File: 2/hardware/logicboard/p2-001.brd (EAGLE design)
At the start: 72 x 72 mm, 68 parts, among them IC1 74LS06N, IC101 74LS153D, IC102 LTC485S, IC103 LTC485S, IC2 4066N, J1 MKR, J101 Qwiic, J102 Qwiic, J103 Qwiic, J104 Qwiic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

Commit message: Clean up of schematic.
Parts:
- J20: value (none) -> GPIO
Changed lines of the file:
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@@
 <attribute name="VALUE" x="54.849" y="68.54" size="0.6096" layer="27" font="vector" ratio="20"/>
 </element>
-<element name="J20" library="SparkFun-Connectors" library_urn="urn:adsk.eagle:library:513" package="1X04_1.27MM" package3d_urn="urn:adsk.eagle:package:38086/1" value="" x="25.65" y="69" smashed="yes">
+<element name="J20" library="SparkFun-Connectors" library_urn="urn:adsk.eagle:library:513" package="1X04_1.27MM" package3d_urn="urn:adsk.eagle:package:38086/1" value="GPIO" x="25.65" y="69" smashed="yes">
 <attribute name="NAME" x="24" y="69" size="1" layer="25" ratio="20" rot="R90" align="center"/>
 <attribute name="VALUE" x="25.142" y="67.349" size="0.6096" layer="27" font="vector" ratio="20"/>

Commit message: Trying to add 4-pin front con.
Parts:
- removed JP5: PWR, pinhead:1X03
- removed V+, VIN: (no value), wirepad:SMD1,27-2,54
- added JP4: (no value), pinhead:1X04
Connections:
- net GND: now also JP4.1, JP4.4; no longer JP5.1
- net LED0: now also JP4.3
- net RST: now also JP4.2
- net V+: no longer JP5.3, V+.1
- net VCC: no longer JP5.2
- net VIN: no longer VIN.1
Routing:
- net GND: track 424.4 -> 0.00 mm, vias 4 -> 0
- net VCC: track 400.8 -> 0.00 mm, vias 18 -> 0
- net SDA: track 214.5 -> 0.00 mm, vias 5 -> 0
- net SCL: track 180.4 -> 0.00 mm, vias 9 -> 0
- net V+: track 149.6 -> 0.00 mm, vias 2 -> 0
- net THS: track 120.9 -> 0.00 mm, vias 4 -> 0
- net MRX+: track 119.0 -> 0.00 mm, vias 4 -> 0
- net MISO: track 117.0 -> 0.00 mm, vias 1 -> 0
- net MIN: track 114.1 -> 0.00 mm, vias 6 -> 0
- net RST: track 112.5 -> 0.00 mm, vias 9 -> 0
- net SCK: track 111.7 -> 0.00 mm, vias 3 -> 0
- net LED0A: track 110.6 -> 0.00 mm, vias 2 -> 0
- net MOSI: track 107.5 -> 0.00 mm, vias 1 -> 0
- net VOUT: track 100.4 -> 0.00 mm, vias 2 -> 0
- net RX: track 95.9 -> 0.00 mm, vias 3 -> 0
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- removed copper zone on layer 1, net GND
- removed copper zone on layer 16, net GND
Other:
- board text added: "2.8.0-RC"
- board text added: "L"
- board text removed: "2.7.1-GM"
- board text removed: "PWR"

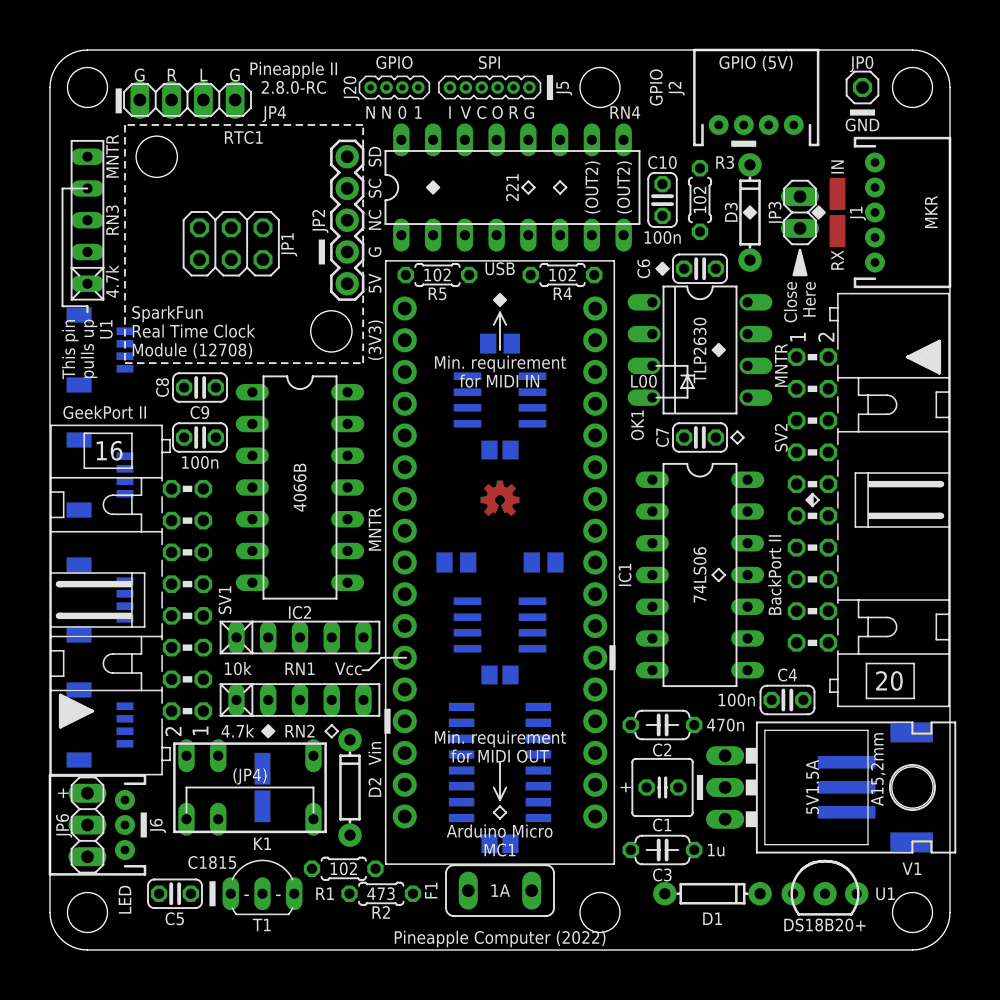
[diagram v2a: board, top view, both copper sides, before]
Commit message: LEDSW connector (temporarily named JP4) is added.
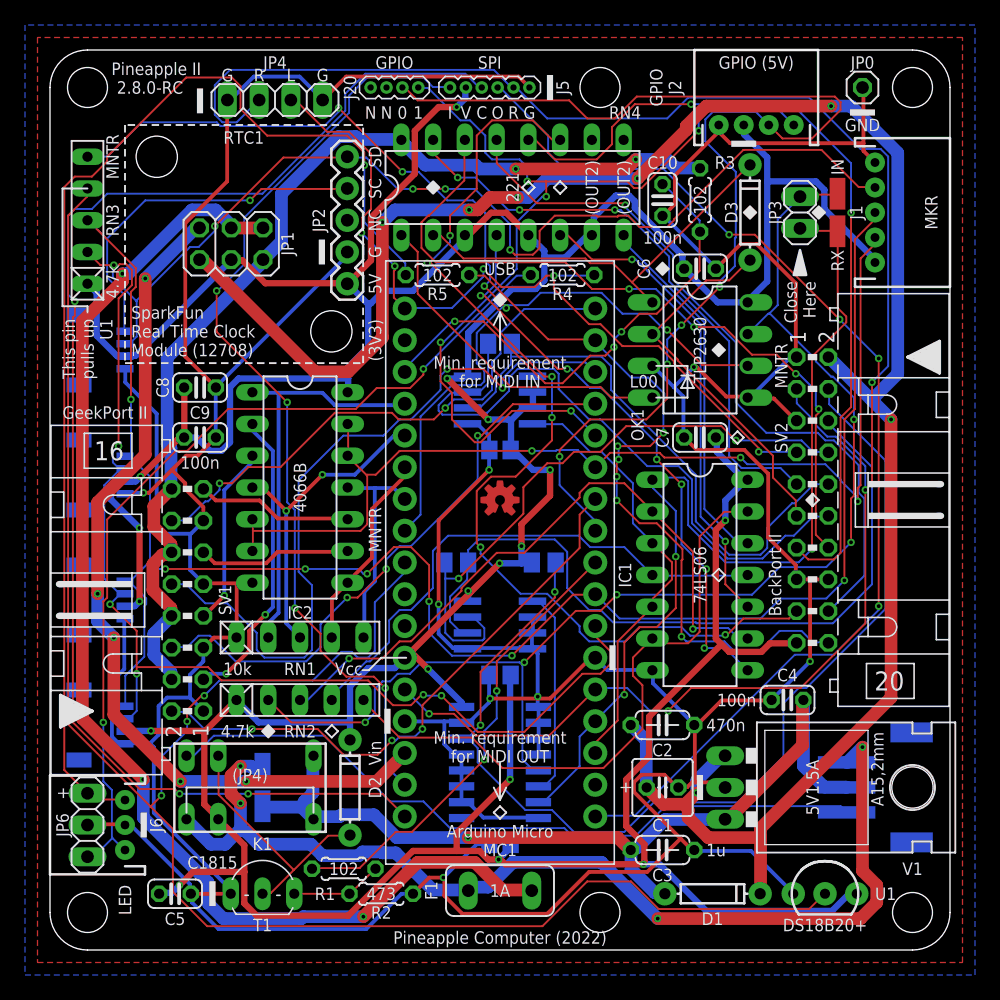
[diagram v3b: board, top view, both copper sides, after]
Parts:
- JP4: value (none) -> LEDSW
- moved JP4 7.00 mm to (18.0, 68.0)
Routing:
- net GND: track 0.00 -> 450.4 mm, vias 0 -> 8
- net VCC: track 0.00 -> 402.6 mm, vias 0 -> 17
- net SDA: track 0.00 -> 174.7 mm, vias 0 -> 10
- net SCL: track 0.00 -> 174.1 mm, vias 0 -> 8
- net V+: track 0.00 -> 167.7 mm, vias 0 -> 7
- net RST: track 0.00 -> 158.0 mm, vias 0 -> 4
- net THS: track 0.00 -> 151.0 mm, vias 0 -> 3
- net SCK: track 0.00 -> 109.6 mm, vias 0 -> 3
- net MIN: track 0.00 -> 101.0 mm, vias 0 -> 5
- net VOUT: track 0.00 -> 99.1 mm, vias 0 -> 3
- net LED1A: track 0.00 -> 95.1 mm, vias 0 -> 1
- net GPIO0: track 0.00 -> 94.1 mm, vias 0 -> 4
- net MNTR: track 0.00 -> 91.8 mm, vias 0 -> 5
- net MOSI: track 0.00 -> 90.0 mm, vias 0 -> 4
- net D7GATE: track 0.00 -> 85.4 mm, vias 0 -> 3
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- added copper zone on layer 1, net GND
- added copper zone on layer 16, net GND

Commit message: Extra I2C conn.
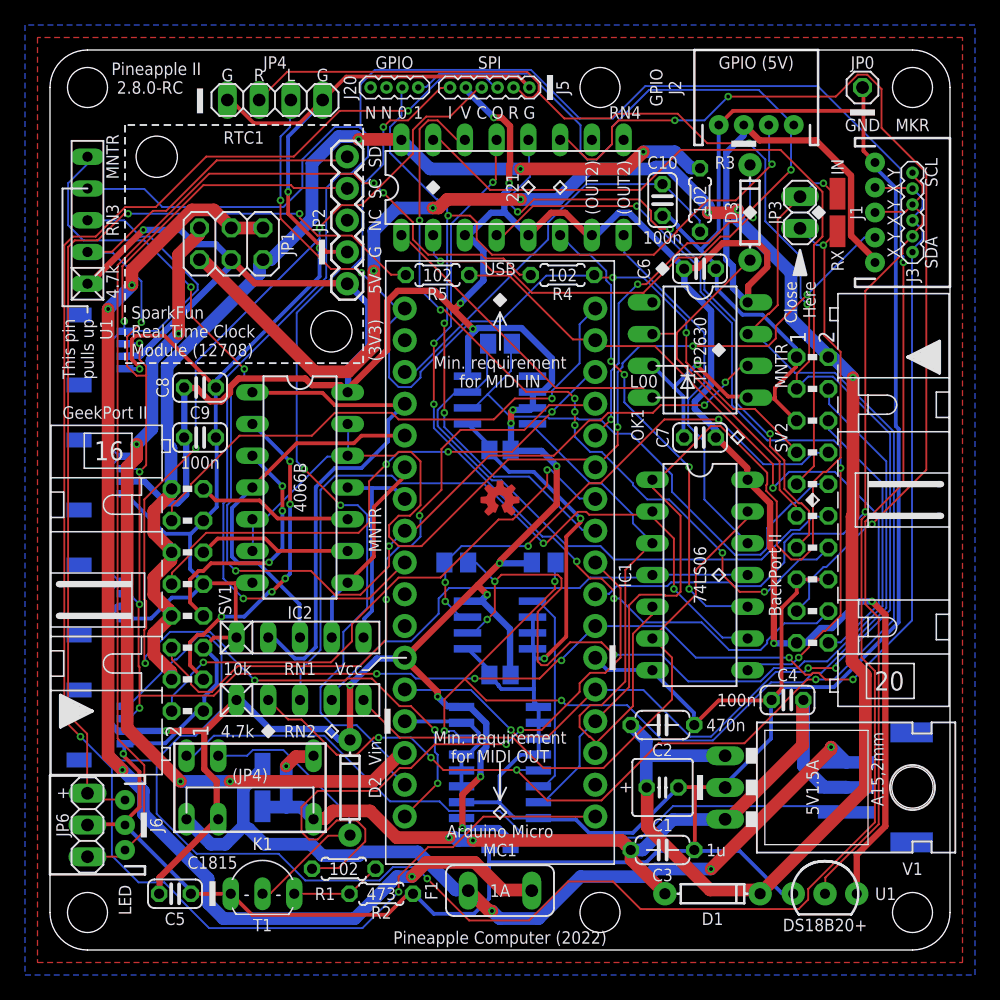
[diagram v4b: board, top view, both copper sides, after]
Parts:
- added J3: I2C, SparkFun-Connectors:1X06_1.27MM
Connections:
- net SCL: now also J3.2, J3.4, J3.6
- net SDA: now also J3.1, J3.3, J3.5
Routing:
- net SCL: track 174.1 -> 264.2 mm, vias 8 -> 3
- net THS: track 151.0 -> 198.6 mm, vias 3 -> 2
- net MOSI: track 90.0 -> 136.5 mm, vias 4 -> 3
- net LED0A: track 72.2 -> 91.8 mm
- net RST: track 158.0 -> 139.6 mm, vias 4 -> 5
- net V+: track 167.7 -> 149.8 mm, vias 7 -> 6
- net MTRTNRAW: track 46.8 -> 64.2 mm, vias 6 -> 3
- net LED1A: track 95.1 -> 77.9 mm, vias 1 -> 2
- net RLY: track 36.8 -> 53.7 mm
- net DTCT2: track 59.1 -> 43.6 mm, vias 2 -> 3
- net VOUTRAW2: track 84.4 -> 69.1 mm, vias 4 -> 3
- net MOSND: track 66.7 -> 51.5 mm, vias 2 -> 3
- net VCC: track 402.6 -> 387.9 mm
- net GPIO0: track 94.1 -> 79.5 mm
- net SCK: track 109.6 -> 95.8 mm, vias 3 -> 6
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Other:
- board text added: "X"
- board text added: "Y"
